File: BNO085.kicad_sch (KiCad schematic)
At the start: 7 parts, among them CN1 X1502WR-05K-N0SN, U5 BNO085, Y1 32.768

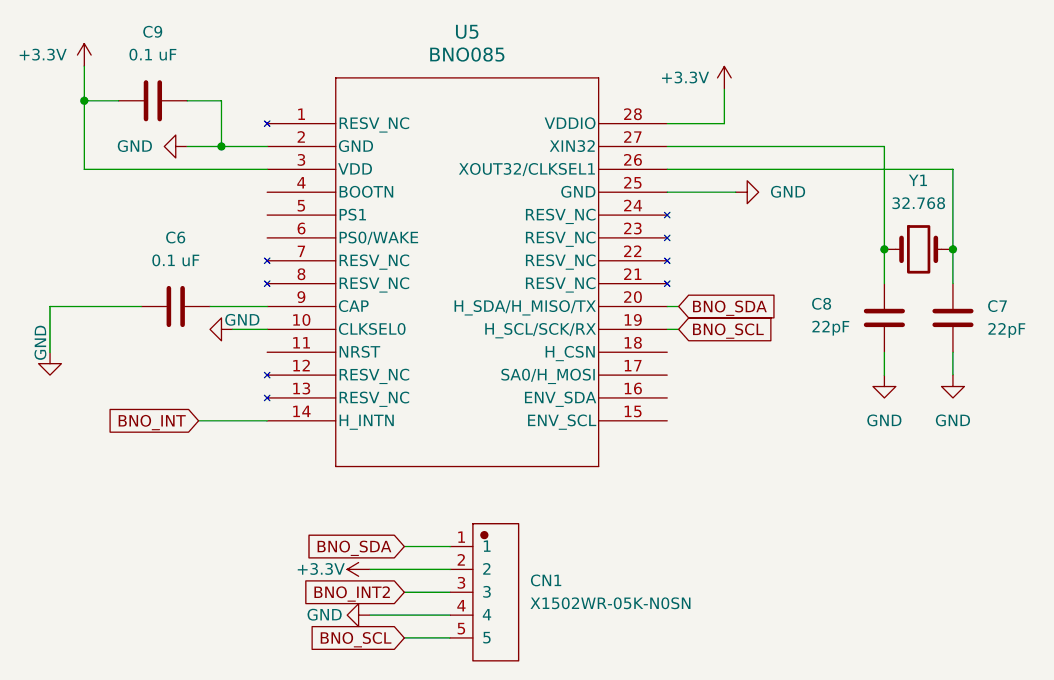
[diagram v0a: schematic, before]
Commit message: Add logo and remove crystal
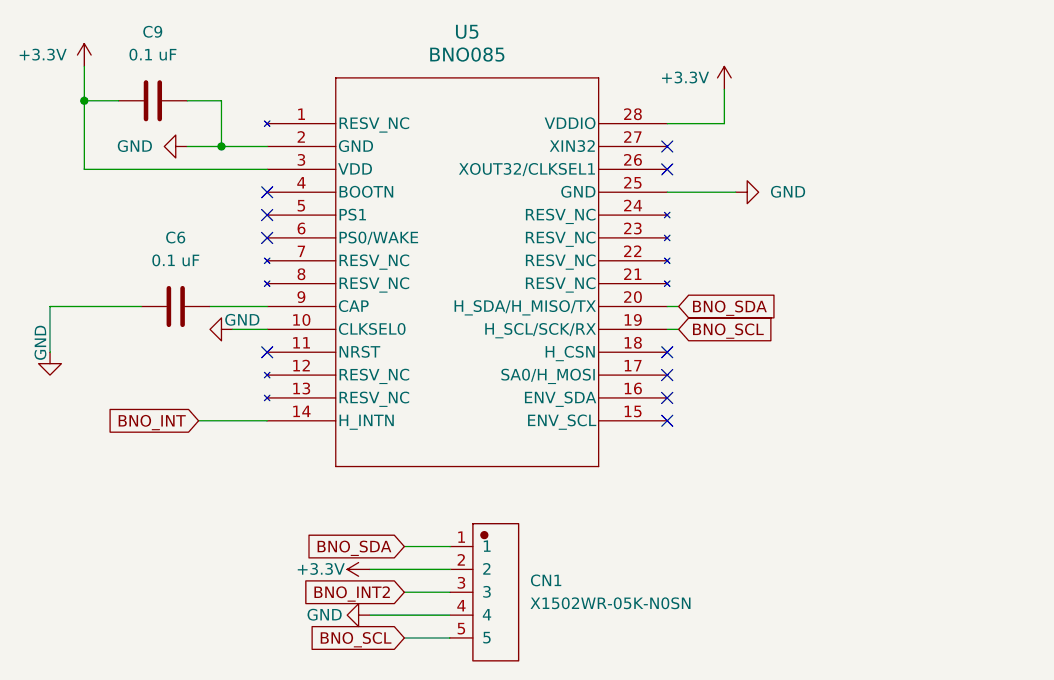
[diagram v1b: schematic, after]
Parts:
- removed C7, C8: 22pF, Capacitor_SMD:C_0402_1005Metric, symbol uSlime:C
- removed Y1: 32.768, uSlime-libs:OSC-SMD_L3.2-W1.5, symbol uSlime:Crystal
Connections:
- no-connect marks 0 -> 10

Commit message: Add NC points
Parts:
- C6, C9: value 0.1 uF -> 0.1uF
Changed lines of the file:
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@@
 			)
 		)
-		(property "Value" "0.1 uF"
+		(property "Value" "0.1uF"
 			(at 105.41 92.71 90)
 			(effects
@@
 			)
 		)
-		(property "Value" "0.1 uF"
+		(property "Value" "0.1uF"
 			(at 102.87 69.85 90)
 			(effects
